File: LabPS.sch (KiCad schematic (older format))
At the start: 57 parts, among them J1 Fan, J2 24Vac, J3 P2, J4 P1, J5 Vo, Q1 BC558, Q2 BD139, Q3 BC548, Q4 2N3055, U1 L7812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

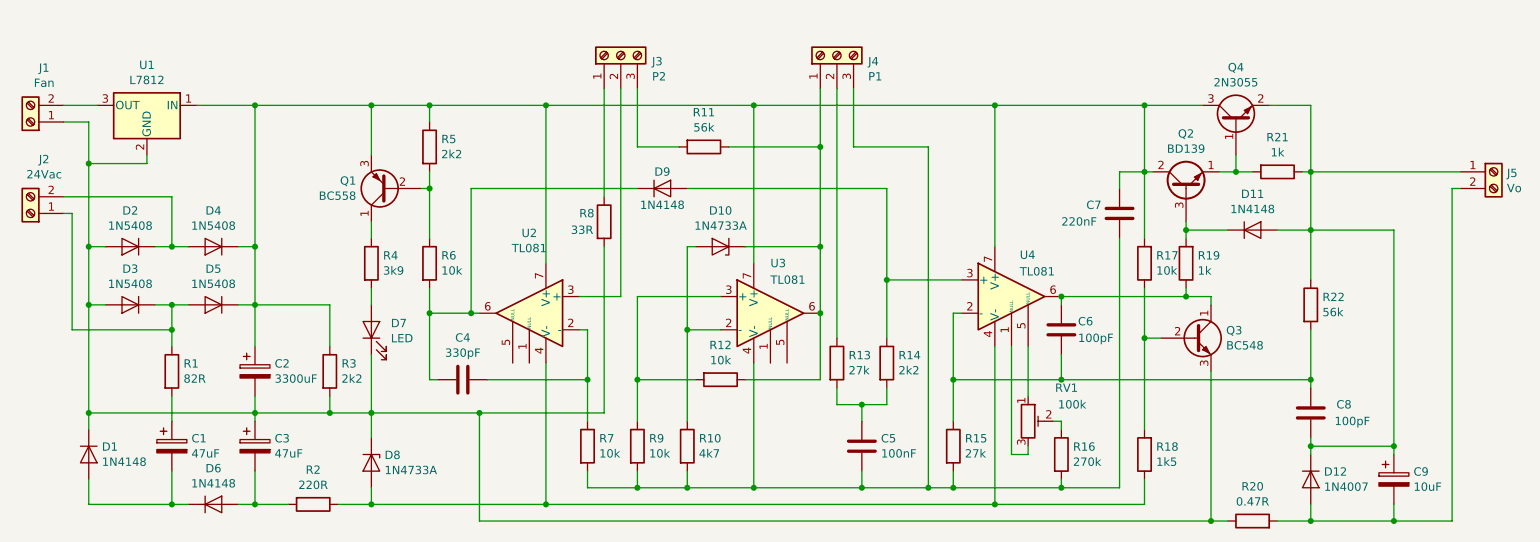
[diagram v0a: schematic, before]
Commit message: Schematic review and footprints added.
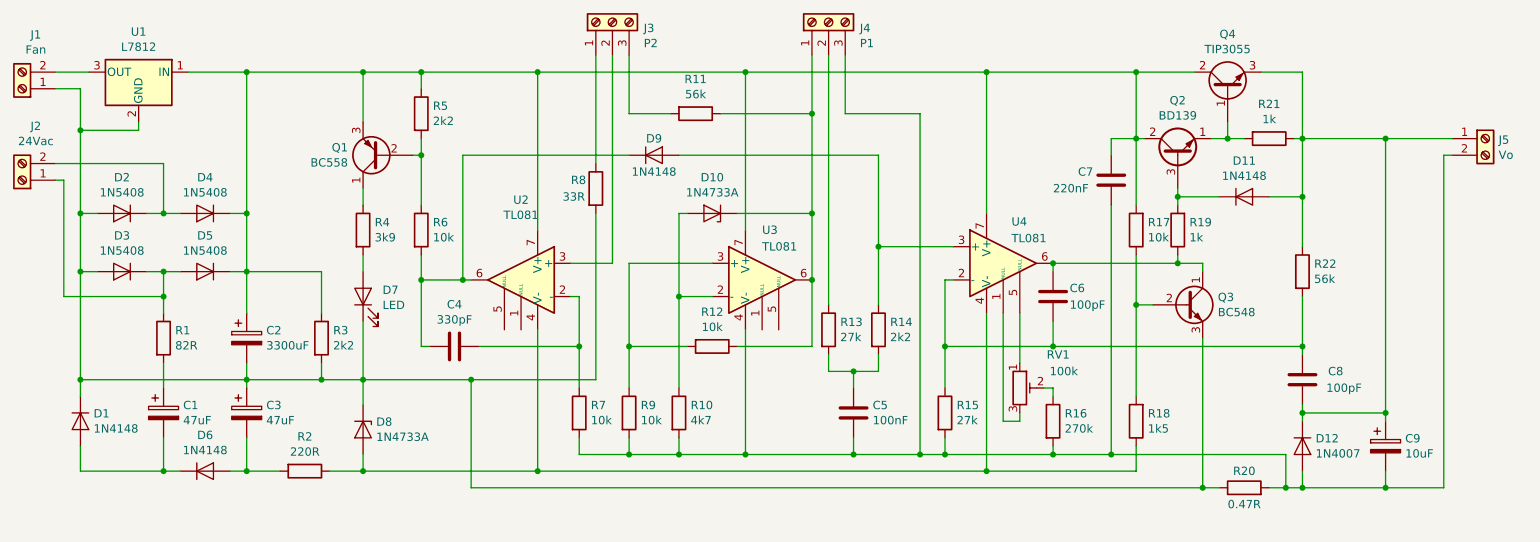
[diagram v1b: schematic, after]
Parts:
- removed Q4: 2N3055, Package_TO_SOT_THT:TO-3, symbol Transistor_BJT:2N3055
- added Q4: TIP3055, Package_TO_SOT_THT:TO-218-3_Vertical, symbol Transistor_BJT:TIP3055
- C1, C3, C9: footprint (none) -> Capacitor_THT:C_Radial_D5.0mm_H11.0mm_P2.00mm
- C2: footprint (none) -> Capacitor_THT:C_Radial_D18.0mm_H35.5mm_P7.50mm
- C4, C6, C8: footprint (none) -> Capacitor_THT:C_Disc_D5.0mm_W2.5mm_P5.00mm
- C5, C7: footprint (none) -> Capacitor_THT:C_Rect_L13.5mm_W5.0mm_P10.00mm_FKS3_FKP3_MKS4
- D7: footprint (none) -> LED_THT:LED_D5.0mm
- J1: footprint (none) -> Connector_PinHeader_2.54mm:PinHeader_1x02_P2.54mm_Vertical
- J2, J5: footprint (none) -> TerminalBlock:TerminalBlock_bornier-2_P5.08mm
- J3, J4: footprint (none) -> Connector_PinHeader_2.54mm:PinHeader_1x03_P2.54mm_Vertical
- R1, R2: footprint (none) -> Resistor_THT:R_Axial_DIN0309_L9.0mm_D3.2mm_P12.70mm_Horizontal
- R10, R11, R12, R13, R14, R15, R16, R17, R18, R19, R21, R22, R4, R5, R6, R7, R8, R9: footprint (none) -> Resistor_THT:R_Axial_DIN0207_L6.3mm_D2.5mm_P10.16mm_Horizontal
- R20: footprint (none) -> Resistor_THT:R_Axial_Power_L25.0mm_W9.0mm_P30.48mm
- R3: footprint (none) -> Resistor_THT:R_Axial_DIN0918_L18.0mm_D9.0mm_P30.48mm_Horizontal
- RV1: footprint (none) -> Potentiometer_THT:Potentiometer_Bourns_3296Z_Horizontal
- U1: footprint (none) -> Package_TO_SOT_THT:TO-220-3_Vertical
- U2, U3, U4: footprint (none) -> Package_DIP:DIP-8_W7.62mm
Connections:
- net at C2.1, C7.2, D4.1 (K)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: now also Q4.2 (C)
- net at C5.1, C7.1, J4.3 (Pin_3)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: now also C9.2, D12.2 (A), J5.2 (Pin_2), R20.2
- net at Q2.1 (E), R21.2: now also Q4.1 (B)
- net at C8.2, C9.1, D11.2 (A)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: now also Q4.3 (E)
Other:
- moved on the sheet: C1, C2, C3, C4, C5, C6, C7, C8, C9, D1, D10, D11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

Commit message: Final PCB layout.
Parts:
- R3: footprint Resistor_THT:R_Axial_DIN0918_L18.0mm_D9.0mm_P30.48mm_Horizontal -> Resistor_THT:R_Axial_DIN0614_L14.3mm_D5.7mm_P15.24mm_Horizontal
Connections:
- net at D3.1 (K), D5.2 (A), R1.1: now also J2.2 (Pin_2); no longer J2.1 (Pin_1)
- net at D2.1 (K), D4.2 (A): now also J2.1 (Pin_1); no longer J2.2 (Pin_2)
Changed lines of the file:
@@
 Wire Wire Line
 	2750 3500 2650 3500
-$Comp
-L Connector:Screw_Terminal_01x02 J2
-U 1 1 5F05E267
-P 1400 3300
-F 0 "J2" H 1318 2975 50  0000 C CNN
-F 1 "24Vac" H 1318 3066 50  0000 C CNN
-F 2 "TerminalBlock:TerminalBlock_bornier-2_P5.08mm" H 1400 3300 50  0001 C CNN
-F 3 "~" H 1400 3300 50  0001 C CNN
-	1    1400 3300
-	-1   0    0    1
-$EndComp
 Wire Wire Line
 	2150 3500 2250 3500
@@
 Wire Wire Line
 	1650 4000 1650 3300
-Wire Wire Line
-	1650 3300 1600 3300
 Connection ~ 2250 3850
 Wire Wire Line
@@
 F 0 "R3" H 3270 4296 50  0000 L CNN
 F 1 "2k2" H 3270 4205 50  0000 L CNN
-F 2 "Resistor_THT:R_Axial_DIN0918_L18.0mm_D9.0mm_P30.48mm_Horizontal" V 3130 4250 50  0001 C CNN
+F 2 "Resistor_THT:R_Axial_DIN0614_L14.3mm_D5.7mm_P15.24mm_Horizontal" V 3130 4250 50  0001 C CNN
 F 3 "~" H 3200 4250 50  0001 C CNN
 	1    3200 4250
@@
 	9100 4000 9100 4300
 Wire Wire Line
-	1600 3200 2250 3200
-Wire Wire Line
 	10000 3050 9600 3050
 $Comp
@@
 	0    -1   -1   0
 $EndComp
+Wire Wire Line
+	1650 3300 1600 3300
+Wire Wire Line
+	1600 3200 2250 3200
+$Comp
+L Connector:Screw_Terminal_01x02 J2
+U 1 1 5F05E267
+P 1400 3200
+F 0 "J2" H 1318 2875 50  0000 C CNN
+F 1 "24Vac" H 1318 2966 50  0000 C CNN
+F 2 "TerminalBlock:TerminalBlock_bornier-2_P5.08mm" H 1400 3200 50  0001 C CNN
+F 3 "~" H 1400 3200 50  0001 C CNN
+	1    1400 3200
+	-1   0    0    -1
+$EndComp
 $EndSCHEMATC
